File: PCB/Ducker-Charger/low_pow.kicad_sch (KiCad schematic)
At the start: 0 parts

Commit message: feat: STPD01 setup
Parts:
- added C, C28: 4.7u 50V, symbol Device:C
- added CBOOT: 100n 50V, symbol Device:C
- added CCDC: 4.7n, symbol Device:C
- added Cin: 10u 50V, symbol Device:C
- added Cout1, Cout2: 22u 25V, symbol Device:C
- added J4: Conn_01x02, symbol Connector_Generic:Conn_01x02
- added L3: 10u, symbol Device:L
- added Q11, Q8: AO4407A, EasyEDA:SOIC-8_L4.9-W3.9-P1.27-LS6.0-BL, symbol EasyEDA:AO4407A
- added Q12, Q9: AO3400A, EasyEDA:SOT-23-3_L2.9-W1.3-P1.90-LS2.4-BR, symbol EasyEDA:AO3400A
- added R23, R27: 10k, symbol Device:R
- added R25, R26, Ron: 100k, symbol Device:R
- added RCDC1: 5.6k, symbol Device:R
- added Rsns: 10m, symbol Device:R
- added U3: STPD01PUR, EasyEDA:QFN-24_L4.0-W3.0-P0.40-TL-EP, symbol EasyEDA:STPD01PUR
- added U5, U6: TPS54302, Package_TO_SOT_SMD:SOT-23-6, symbol Regulator_Switching:TPS54302
- added USBC2: TYPE-C-31-M-12, EasyEDA:USB-C_SMD-TYPE-C-31-M-12_1, symbol EasyEDA:TYPE-C-31-M-12
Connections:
- new net: Q12.1 (G), R26.1, R27.2
- new net: C.1, U3.18 (VREG)
- new net: Q8.4 (G), Q9.3 (D)
- new net: CBOOT.1, U3.16 (BOOT)
- new net: CBOOT.2, L3.1, U3.13 (LX), U3.14 (LX), U3.15 (LX)
- new net: Q11.4 (G), Q12.3 (D)
- new net: Q9.1 (G), R23.2, R25.1
- new net: Ron.1, U3.17 (Pon)
- new net: CCDC.1, RCDC1.1, U3.21 (VSNS)
- new net: Cout1.1, L3.2, Rsns.1, U3.19 (ISNS+)
- new net: C28.1, U3.6 (VDRIVEH)
- new net BATT_+: Cin.1, Ron.2, U3.8 (PVIN), U3.9 (PVIN)
- new net CC1: USBC2.A5 (CC1)
- new net CC2: USBC2.B5 (CC2)
- new net DN: USBC2.A7 (DN1), USBC2.B7 (DN2)
- new net DP: USBC2.A6 (DP1), USBC2.B6 (DP2)
- new net GND: C.2, C28.2, Cin.2, Cout1.2, Cout2.2, J4.2 (Pin_2), Q12.2 (S), Q9.2 (S), U3.10 (PGND), U3.11 (PGND), U3.12 (PGND), U3.24 (SGND), U3.25 (EP), U3.3 (ADD), USBC2.1 (EH), USBC2.2 (EH), USBC2.3 (EH), USBC2.4 (EH), USBC2.A1B12 (GND), USBC2.B1A12 (GND)
- new net I2C1_SCL: U3.2 (SCL)
- new net I2C1_SDA: U3.1 (SDA)
- new net LAB_2ENABLER: R27.1
- new net LP_ST_EN: U3.5 (EN)
- new net LP_ST_INT: U3.4 (INT)
- new net USB_C_2ENABLER: R23.1
- new net VBUS: Q8.5 (D), Q8.6 (D), Q8.7 (D), Q8.8 (D), USBC2.A4B9 (VBUS), USBC2.B4A9 (VBUS)
- new net V_LABS: J4.1 (Pin_1), Q11.5 (D), Q11.6 (D), Q11.7 (D), Q11.8 (D)
- new net V_OUT_AUX: CCDC.2, Cout2.1, Q11.1 (S), Q11.2 (S), Q11.3 (S), Q8.1 (S), Q8.2 (S), Q8.3 (S), R25.2, R26.2, RCDC1.2, Rsns.2, U3.20 (ISNS-)
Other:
- note added: "Shielded, >4A saturation"
- note added: "USB-C CONTROLLER"
- note added: "USB-C INTERFACE"
- note added: "check polarity; may be reversed (D-S)"

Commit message: feat: added STUSB4710AQ1TR
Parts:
- added C30, C31: 1u, symbol Device:C
- added IC4: STUSB4710AQ1TR, QFN50P300X300X65-16N, symbol STUSB4710AQ1TR:STUSB4710AQ1TR
- added Q7: AO3400A, EasyEDA:SOT-23-3_L2.9-W1.3-P1.90-LS2.4-BR, symbol EasyEDA:AO3400A
- added R24: 510k, symbol Device:R
- added R28: 100k, symbol Device:R
- added R29: 1k2, symbol Device:R
- added R30: 50, symbol Device:R
- renumbered C to C29, CBOOT to CBOOT1, CCDC to CCDC1, Cin to Cin1, Ron to Ron1, Rsns to Rsns2
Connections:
- net BATT_+: now also IC4.1 (VDD), R24.1
- net CC1: now also IC4.2 (CC1)
- net CC2: now also IC4.3 (CC2)
- net GND: now also C30.2, C31.2, IC4.6 (GND), IC4.9 (ADDR0), Q7.2 (S), R28.2
- net VBUS: now also R29.2, R30.2
- net I2C1_SCL renamed SCL
- net SCL: now also IC4.4 (SCL)
- net I2C1_SDA renamed SDA
- net SDA: now also IC4.5 (SDA)
- new net: C30.1, IC4.16 (VREG_2V7)
- new net: C31.1, IC4.15 (VREG_1V2)
- new net: Q7.1 (G), R24.2, R28.1
- new net: IC4.12 (VBUS_SENSE), R29.1
- new net: IC4.13 (VBUS_DISCH), R30.1
- new net C2_RDY: IC4.14 (VBUS_EN_SRC)
- new net USB_A1_EN: Q7.3 (D)
- no-connect marks 0 -> 4
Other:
- note added: "MODE Controller"
- note added: "MODE LAB"
- note added: "MODE USB"
- note added: "USB PD Controller"
- note added: "USB-A1"
- note added: "USB-C2"
- moved on the sheet: C28, C29, CBOOT1, CCDC1, Cin1, Cout1, Cout2, J4, L3, Q11, Q12, Q8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

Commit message: feat: completed low power sheet
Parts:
- added C39, C44: 10u, symbol Device:C
- added C40, C43: 100n, symbol Device:C
- added C41, C42, C45, C46: 22u, symbol Device:C
- added J5, J6: USB_A, symbol Connector:USB_A
- added L4, L5: 10u 5A, symbol Device:L
- added Q13: AO3400A, EasyEDA:SOT-23-3_L2.9-W1.3-P1.90-LS2.4-BR, symbol EasyEDA:AO3400A
- added R35, R37, R39: 100k, symbol Device:R
- added R36, R40: 13.3k, symbol Device:R
- added R38: 1k, symbol Device:R
- added Rshunt, Rshunt1: 10m, symbol Device:R
- added U1: INA3221, Package_DFN_QFN:Texas_RGV0016A_VQFN-16-1EP_4x4mm_P0.65mm_EP2.1x2.1mm, symbol Power_Management:INA3221
- R24: value 510k -> 1k
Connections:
- net BATT_+: now also U5.3 (VIN), U6.3 (VIN), C39.1, C44.1; no longer R24.1
- net GND: now also R28.1, U5.1 (GND), U6.1 (GND), C39.2, C41.2, C42.2, C44.2, C45.2, C46.2, J5.4 (GND), J5.5 (Shield), J6.4 (GND), J6.5 (Shield), Q13.2 (S), R36.2, R39.1, R40.2, U1.17 (EP), U1.3 (GND), U1.5 (A0); no longer R28.2
- net SCL: now also U1.6 (SCL)
- net SDA: now also U1.7 (SDA)
- net USB_A1_EN: now also U5.5 (EN)
- net at Q7.1 (G), R24.2: now also R28.2; no longer R28.1
- net at U5.2 (SW): now also C40.2, L4.1
- net USB_A1_FB: now reaches U5.4 (FB)
- net USB_A1_FB: now also R35.2, R36.1
- net at U5.6 (BOOT): now also C40.1
- net at U6.2 (SW): now also C43.2, L5.1
- net USB_A2_FB: now reaches U6.4 (FB)
- net USB_A2_FB: now also R37.2, R40.1
- net USB_A2_EN: now reaches U6.5 (EN)
- net USB_A2_EN: now also Q13.3 (D)
- net at U6.6 (BOOT): now also C43.1
- new net: Q13.1 (G), R38.2, R39.2
- new net +3V3: U1.4 (VS)
- new net 5V_USB_A1: C41.1, C42.1, L4.2, R35.1, Rshunt.1, U1.12 (IN+1)
- new net 5V_USB_A2: C45.1, C46.1, L5.2, R37.1, Rshunt1.1, U1.15 (IN+2)
- new net IN-1: J5.1 (VBUS), Rshunt.2, U1.11 (IN-1)
- new net IN-2: J6.1 (VBUS), Rshunt1.2, U1.14 (IN-2)
- new net USB_A1_CTRL: R24.1
- new net USB_A2_CTRL: R38.1
- no-connect marks 4 -> 8
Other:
- note added: "BANANA"
- note added: "CURRENT SENSOR"
- note added: "FAILSAFE USBA ENABLER"
- note added: "USB A LINES"
- note added: "USB-A"
- note removed: "USB-A1"
- moved on the sheet: J4, Q7, U5

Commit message: feat: progressed overall schematic
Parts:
- renumbered C28 to C16, C29 to C17, C31 to C18, C30 to C19, C40 to C20, C39 to C21, C41 to C22, C42 to C23, C43 to C24, C44 to C25, C45 to C26, C46 to C27, IC4 to IC1, J4 to J3, J5 to J4, J6 to J5, L3 to L2, L4 to L3, L5 to L4, Q7 to Q10, Q13 to Q11, Q8 to Q6, Q9 to Q7, Q11 to Q8, Q12 to Q9, R29 to R12, R30 to R13, R25 to R14, R23 to R15, R26 to R16, R27 to R17, R24 to R18, R35 to R19, R28 to R20, R36 to R21, R38 to R22, R37 to R23, R39 to R24, R40 to R25, Rshunt to Rshunt1, Rshunt1 to Rshunt2, Rsns2 to Rsns1, U5 to U4, U1 to U5

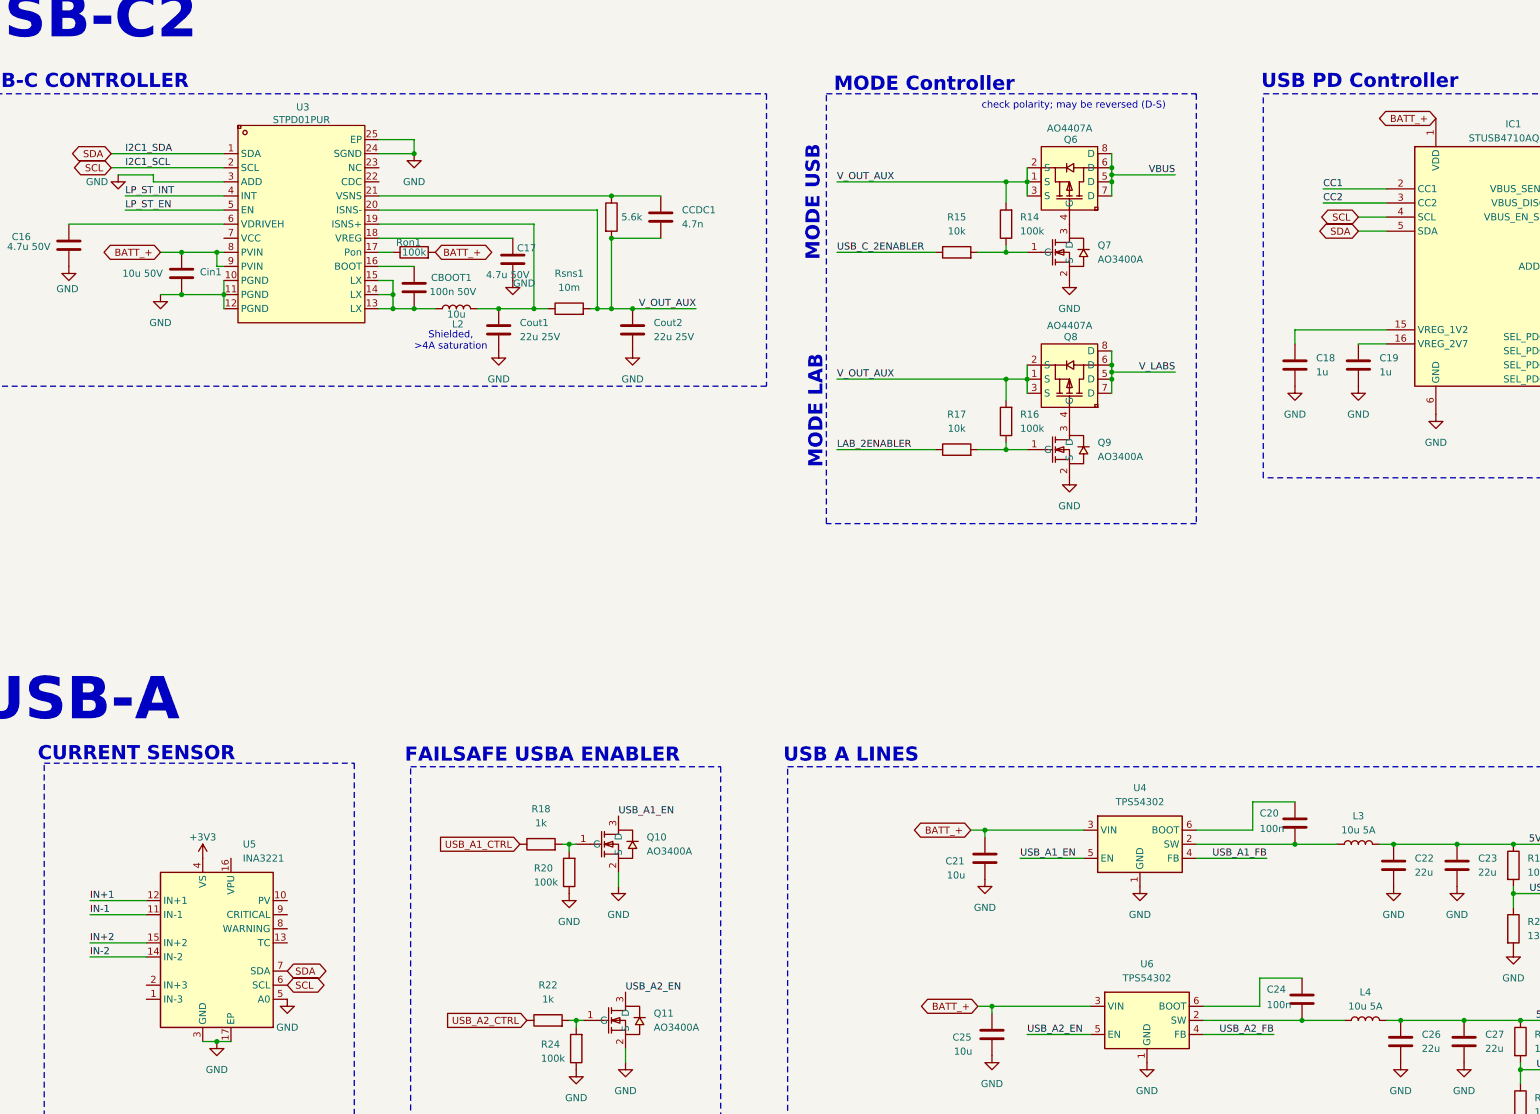
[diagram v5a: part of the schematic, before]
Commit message: fix: power symbols
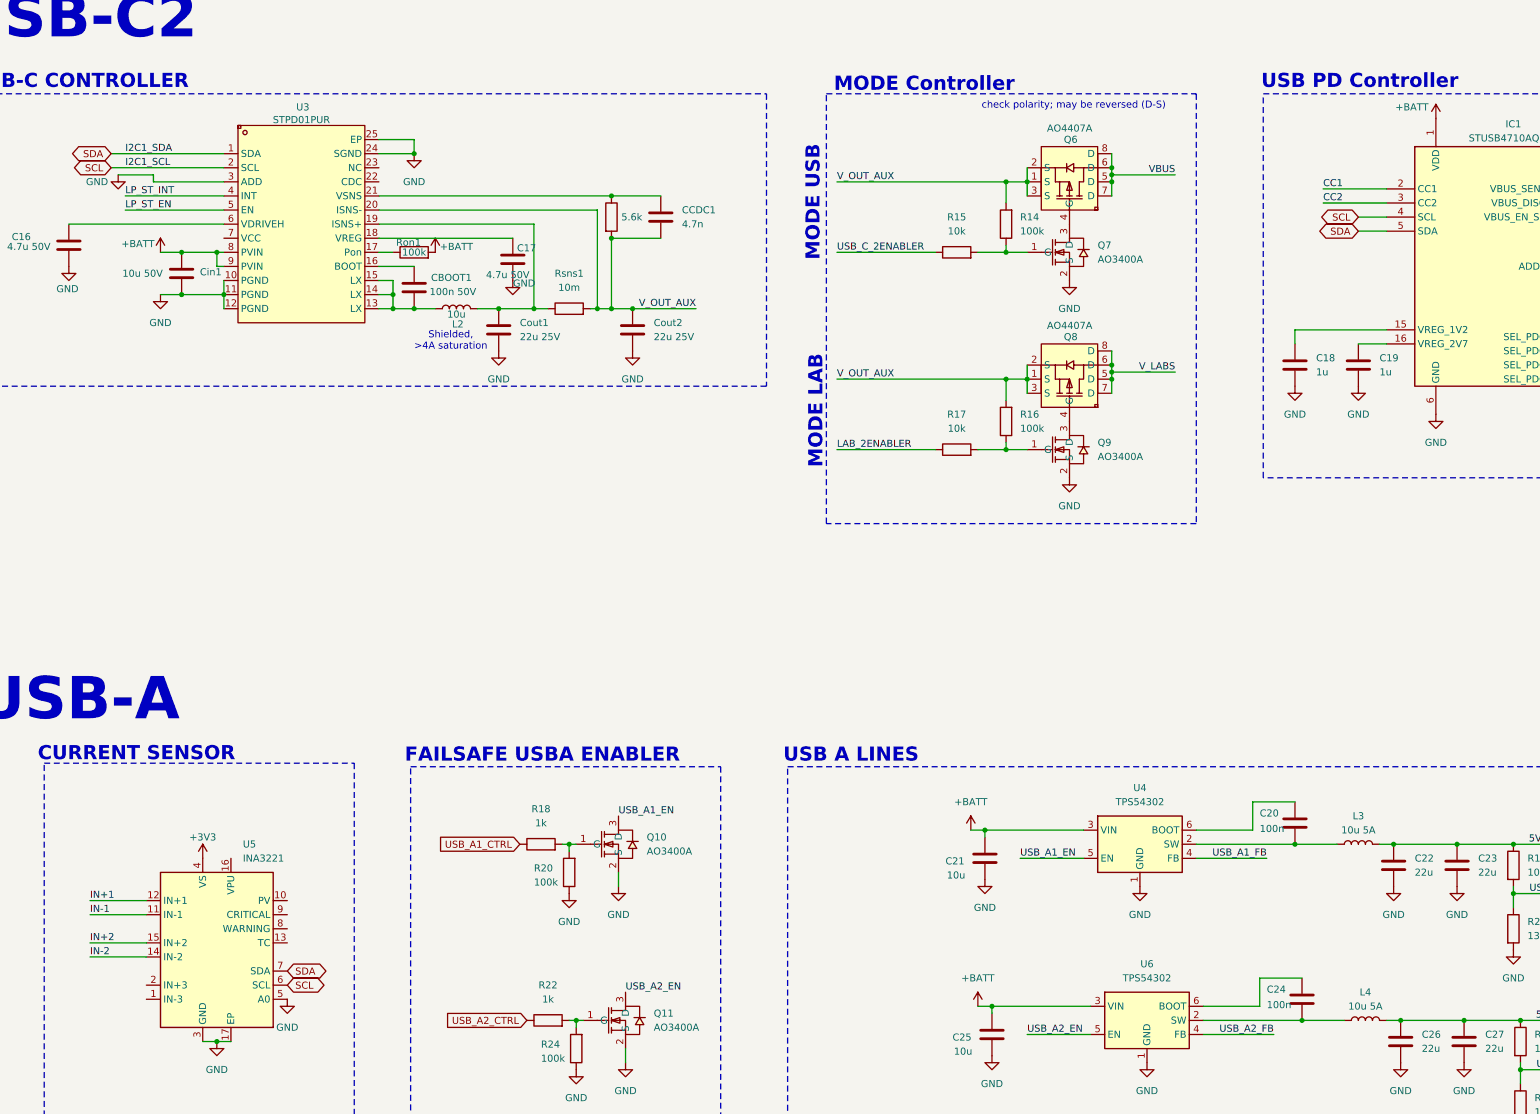
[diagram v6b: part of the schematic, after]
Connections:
- net BATT_+ renamed +BATT

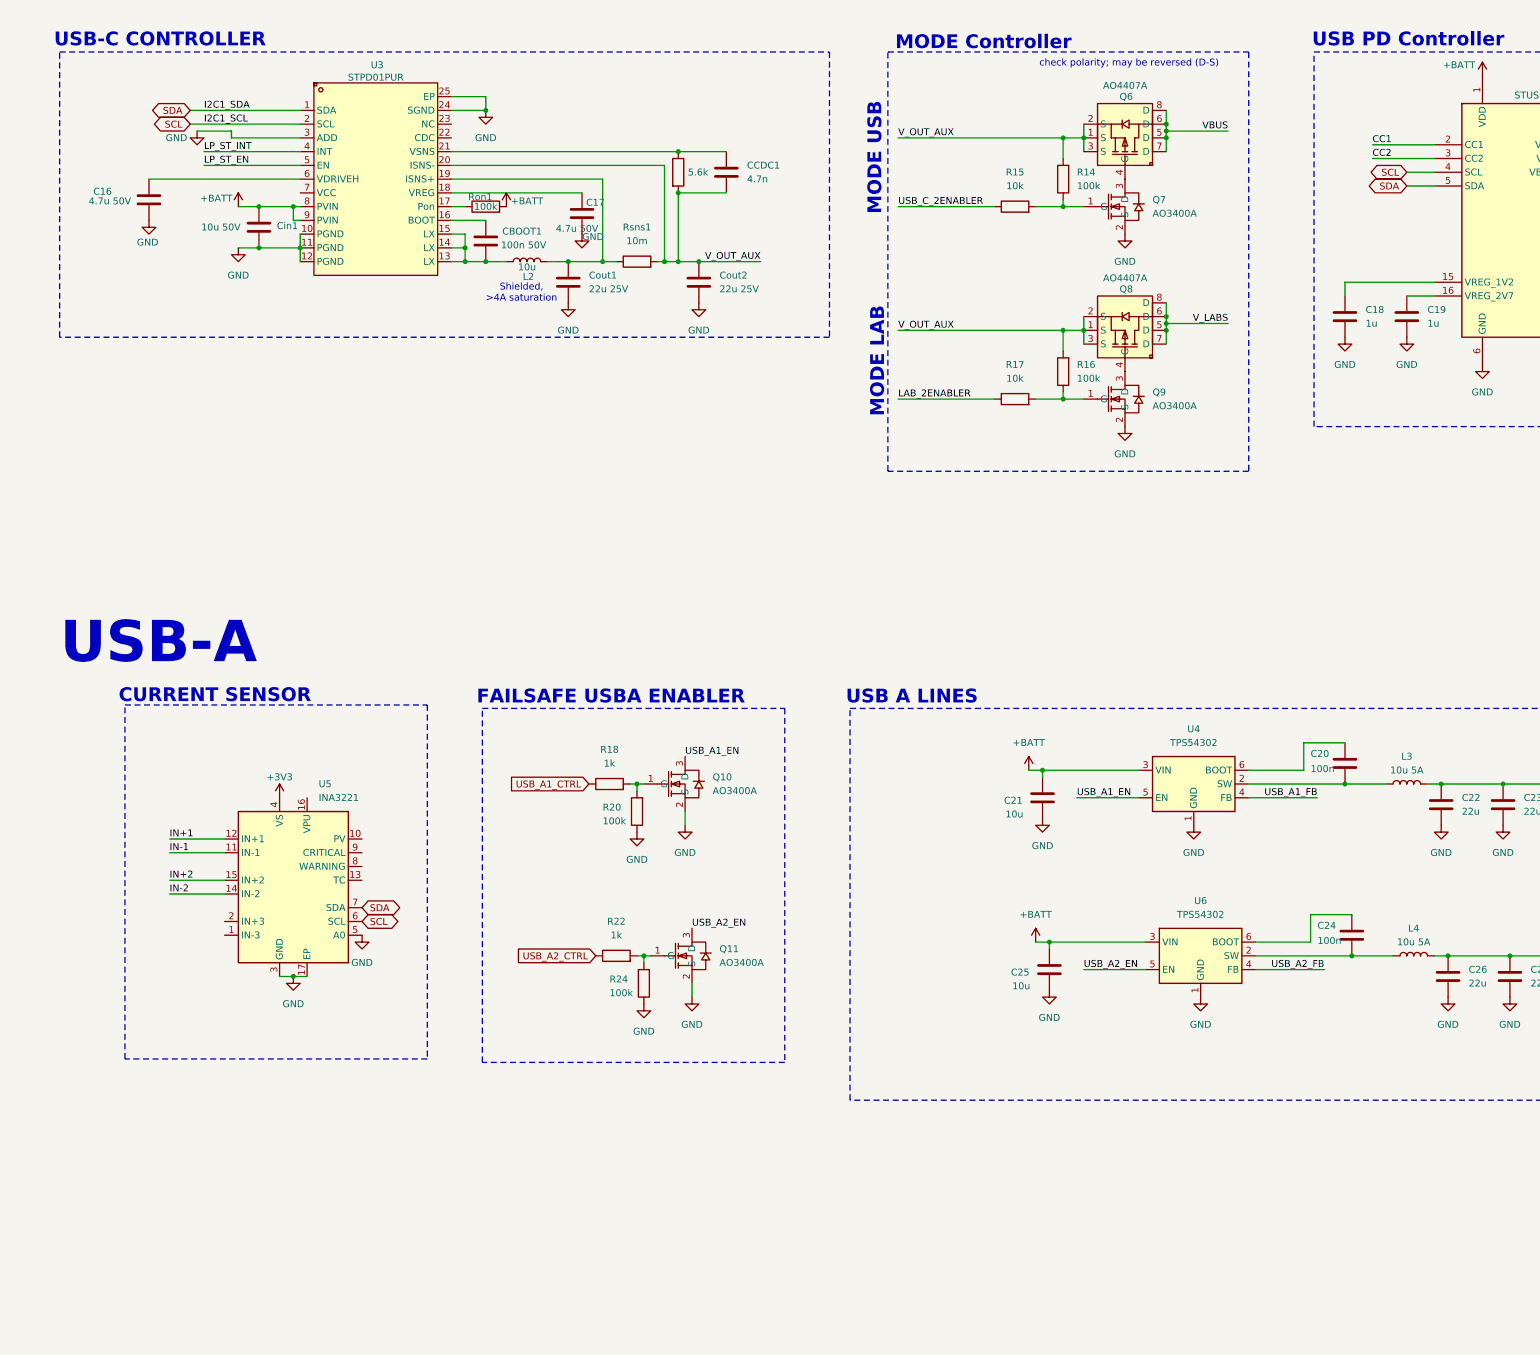
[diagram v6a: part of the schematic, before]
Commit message: fix: I2C is now a BUS, no longer a global label
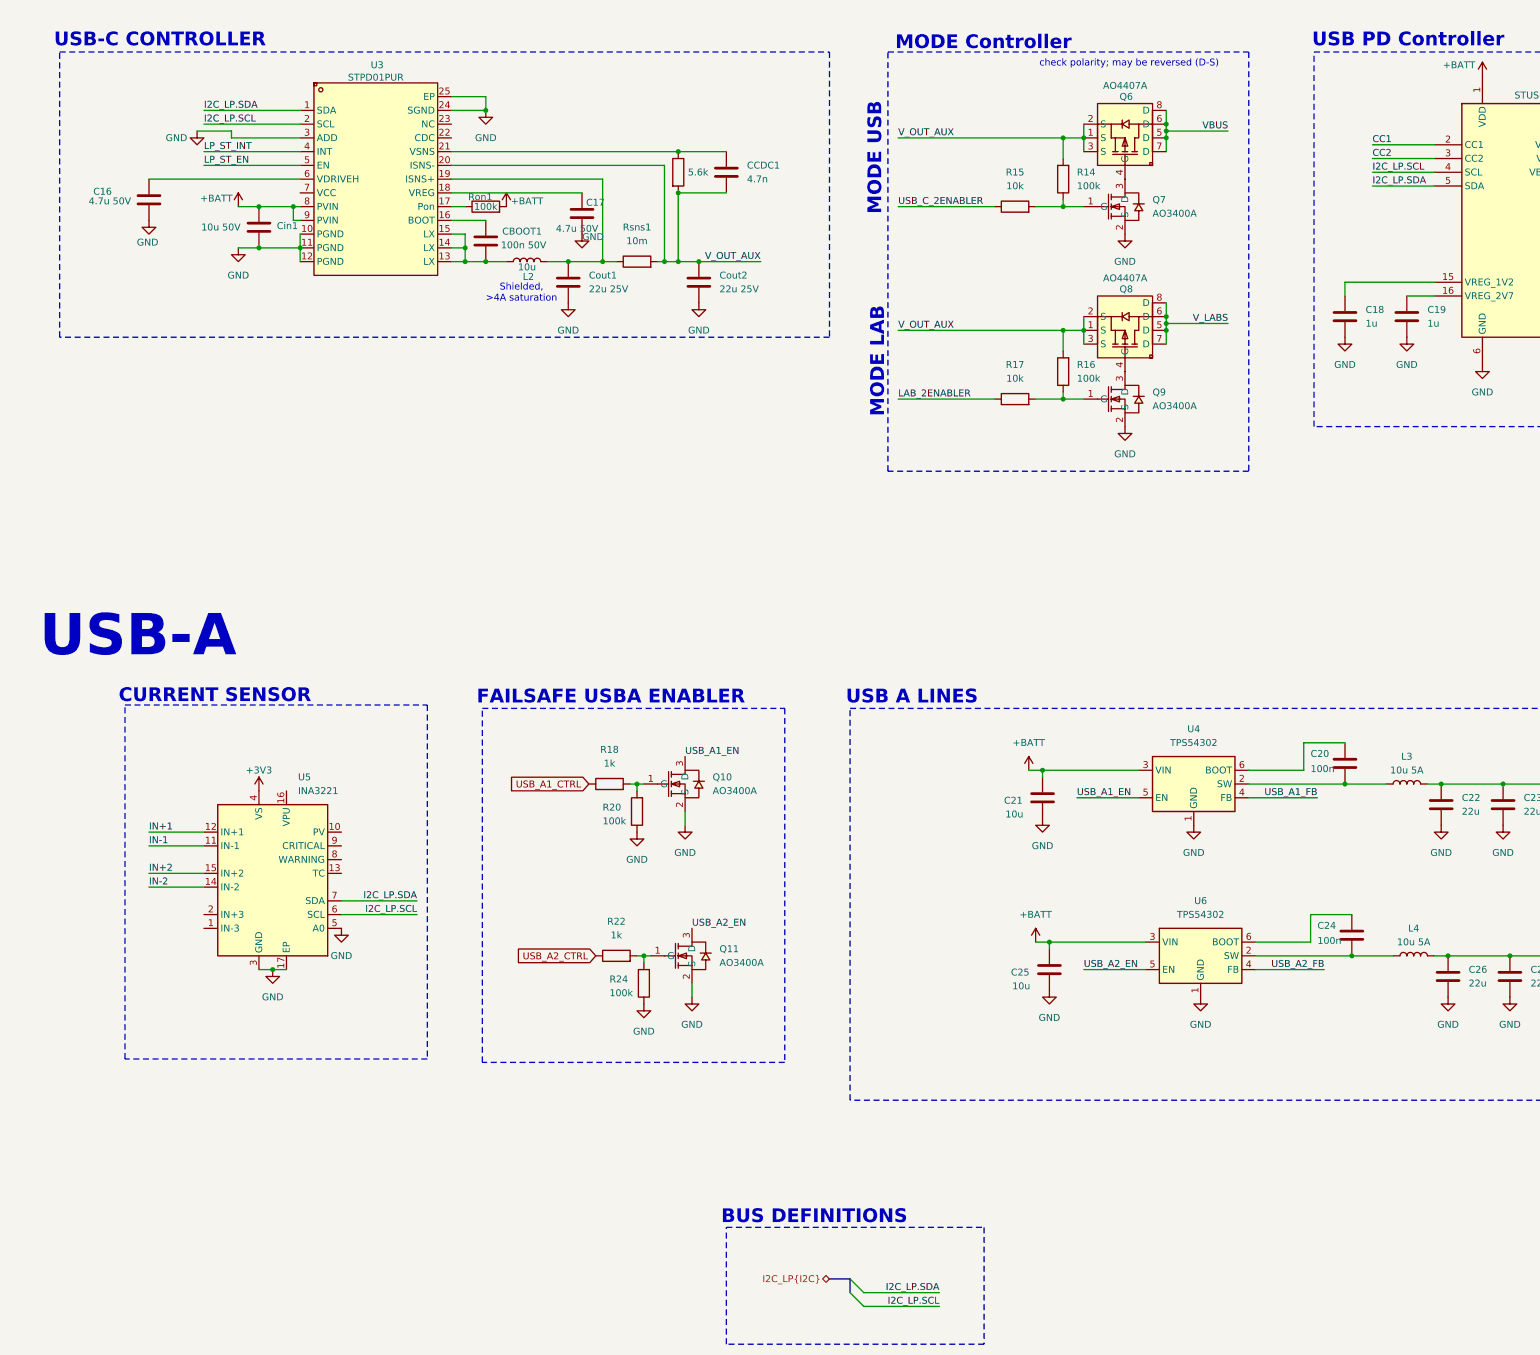
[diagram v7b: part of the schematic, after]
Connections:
- net SCL renamed I2C_LP.SCL
- net SDA renamed I2C_LP.SDA
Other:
- note added: "BUS DEFINITIONS"
- moved on the sheet: U5
